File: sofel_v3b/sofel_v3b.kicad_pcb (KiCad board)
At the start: 2 copper layers, 145.4 x 116.3 mm, 107 parts, among them J1 Pimaroni Trackball, J2 4PIN, J3 OLED, SW1 SW_PUSH_LED, SW10 SW_PUSH_LED, SW11 SW_PUSH_LED, SW12 SW_PUSH_LED, SW13 SW_PUSH_LED, SW14 SW_PUSH_LED, SW15 SW_PUSH_LED, SW16 SW_PUSH_LED, SW17 SW_PUSH_LED, SW18 SW_PUSH_LED, SW19 SW_PUSH_LED, SW2 SW_PUSH_LED, SW20 SW_PUSH_LED, SW21 SW_PUSH_LED, SW22 SW_PUSH_LED, SW23 SW_PUSH_LED, SW24 SW_PUSH_LED, SW25 Rotary_Encoder_Switch, SW26 SW_PUSH_LED, SW27 SW_PUSH_LED, SW28 SW_PUSH_LED, SW29 SW_PUSH_LED, SW3 SW_PUSH_LED, SW30 SW_PUSH_LED, SW4 SW_PUSH_LED, SW5 SW_PUSH_LED, SW6 SW_PUSH_LED, SW7 SW_PUSH_LED, SW8 SW_PUSH_LED, SW9 SW_PUSH_LED, U2 SN74AHCT1G125, U3 Pico

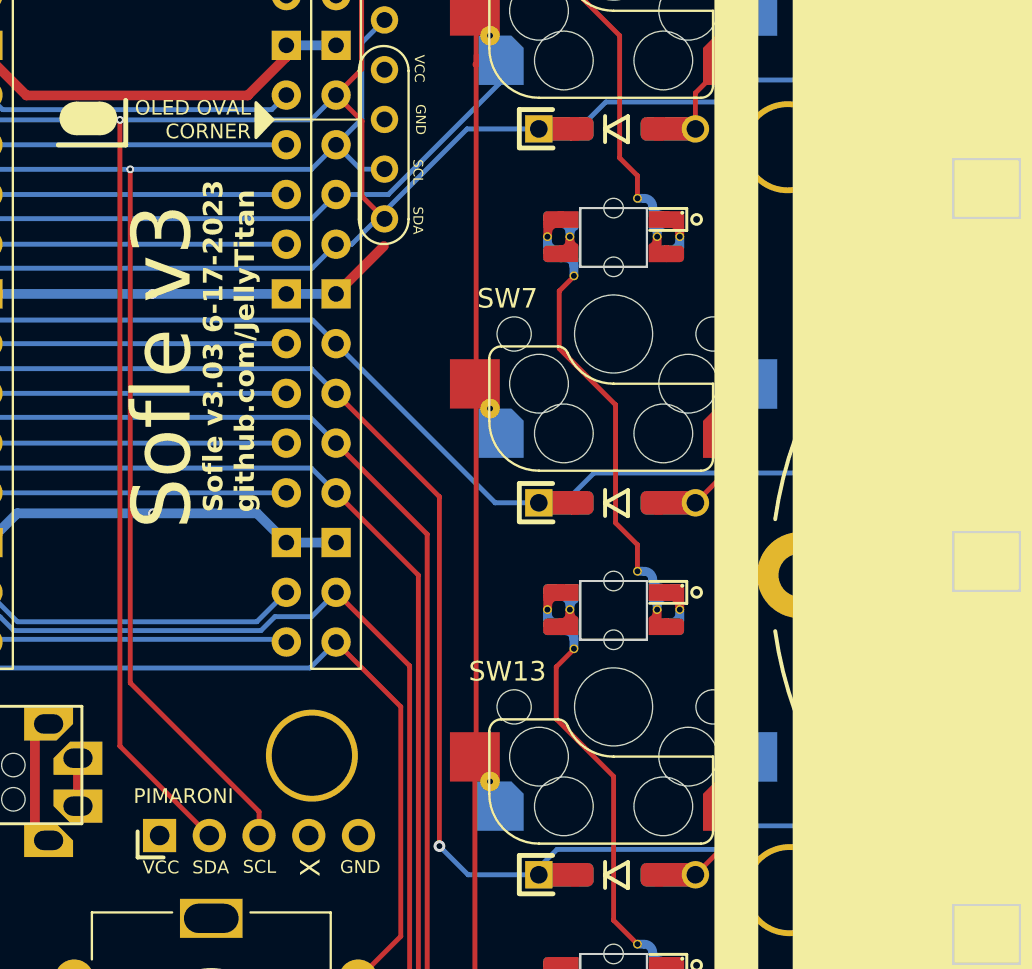
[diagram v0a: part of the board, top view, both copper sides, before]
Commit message: updated keyplate for alternate OLEDs
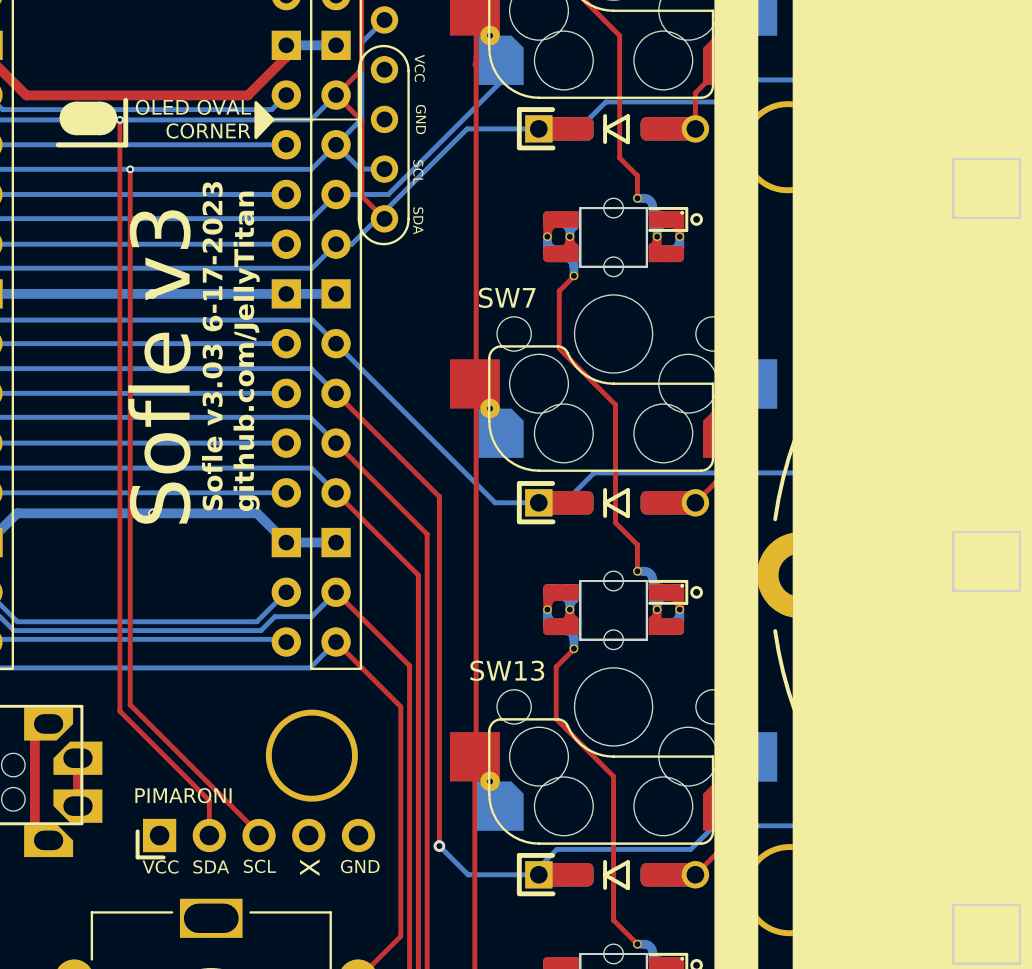
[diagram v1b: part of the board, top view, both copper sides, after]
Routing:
- net GND: track 94.8 -> 91.4 mm

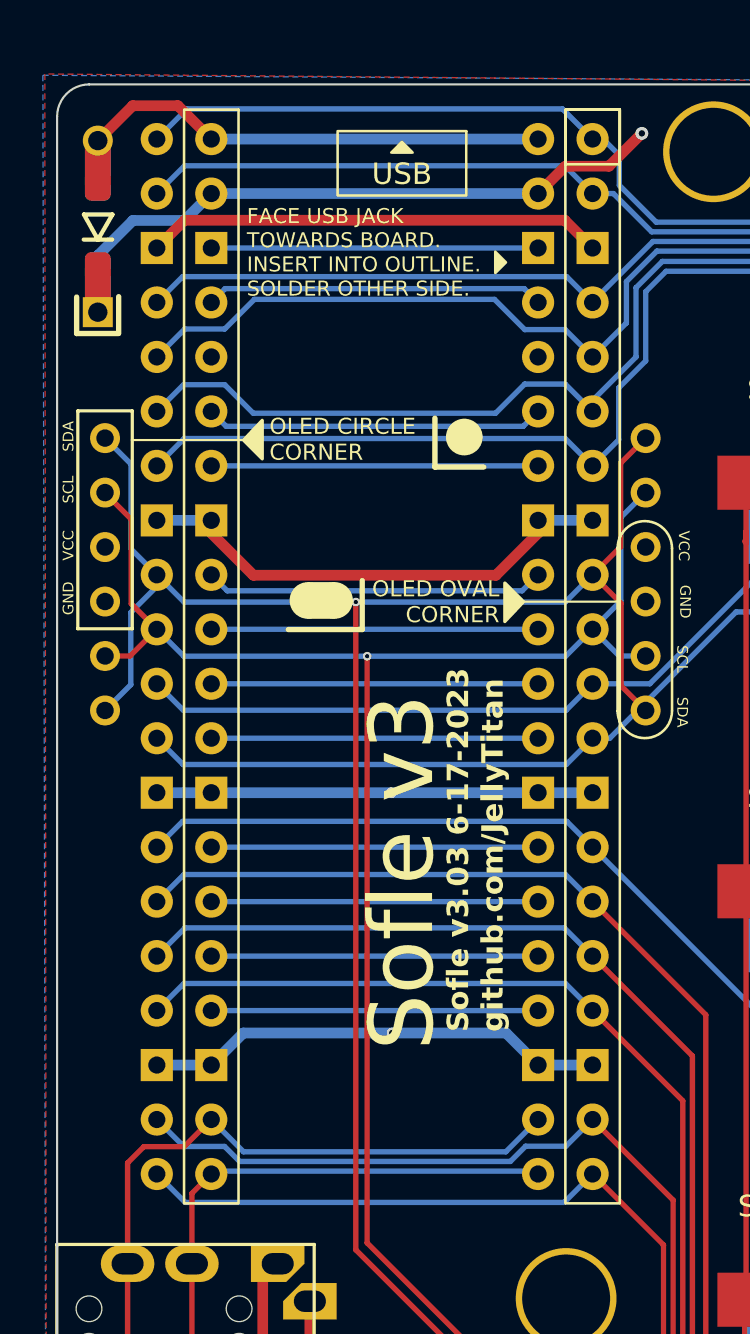
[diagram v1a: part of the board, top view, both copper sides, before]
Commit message: Flipped pico footrpint so buttons face up Removed pcb holes for pico buttons
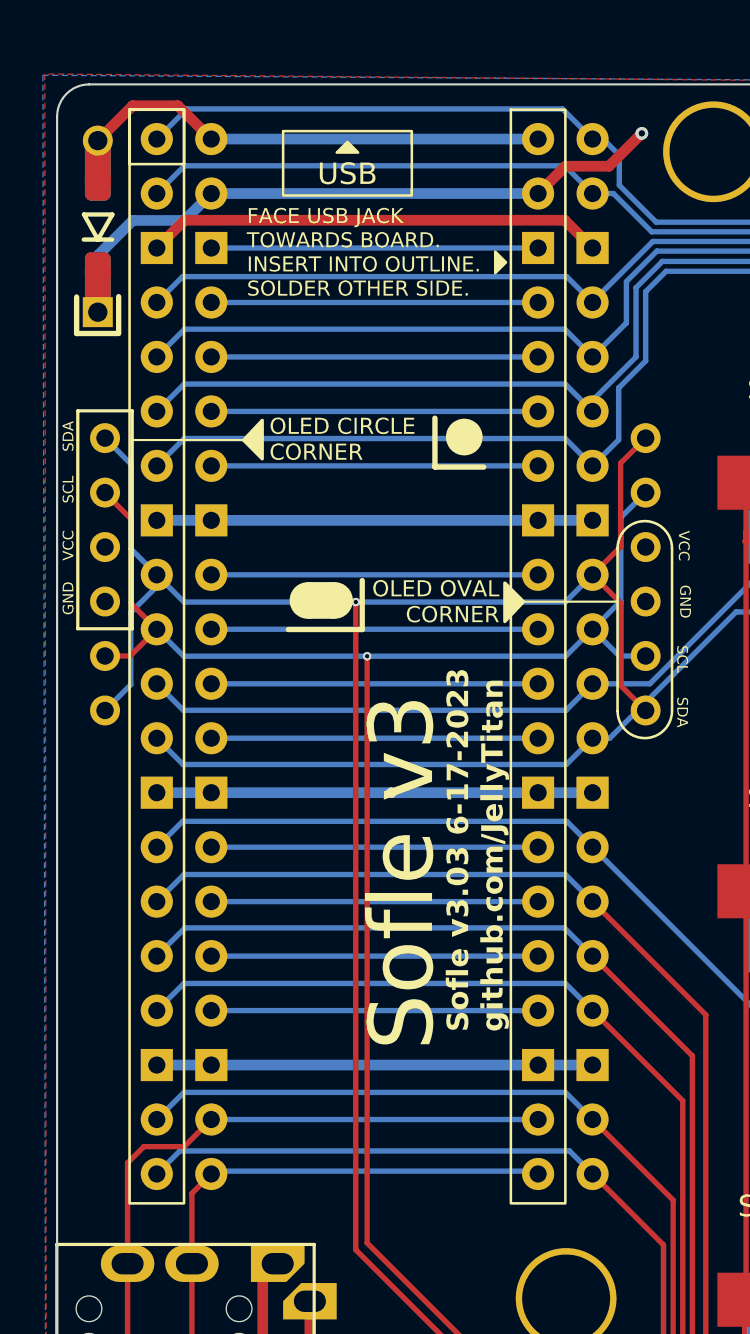
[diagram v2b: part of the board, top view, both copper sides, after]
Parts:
- U3: footprint sofle_v3b:RPi_Pico_SMD_TH - Junco -DS Sofle v3b v4 -> sofle_v3b:RPi_Pico_SMD_TH - Junco -DS Sofle v3b v3 nohole
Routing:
- net unconnected-(U3-3V3-Pad36): track 0.00 -> 15.2 mm
- net GND: track 91.4 -> 87.3 mm, vias 4 -> 3
- net RX: track 31.9 -> 30.6 mm
- net col2: track 215.2 -> 214.0 mm
- net col3: track 201.1 -> 200.0 mm
- net unconnected-(U3-GPIO27_ADC1-Pad32): track 15.9 -> 15.2 mm
- net unconnected-(U3-ADC_VREF-Pad35): track 15.8 -> 15.2 mm
- net ENCA: track 49.3 -> 48.8 mm
- net unconnected-(U3-3V3_EN-Pad37): track 15.8 -> 15.2 mm

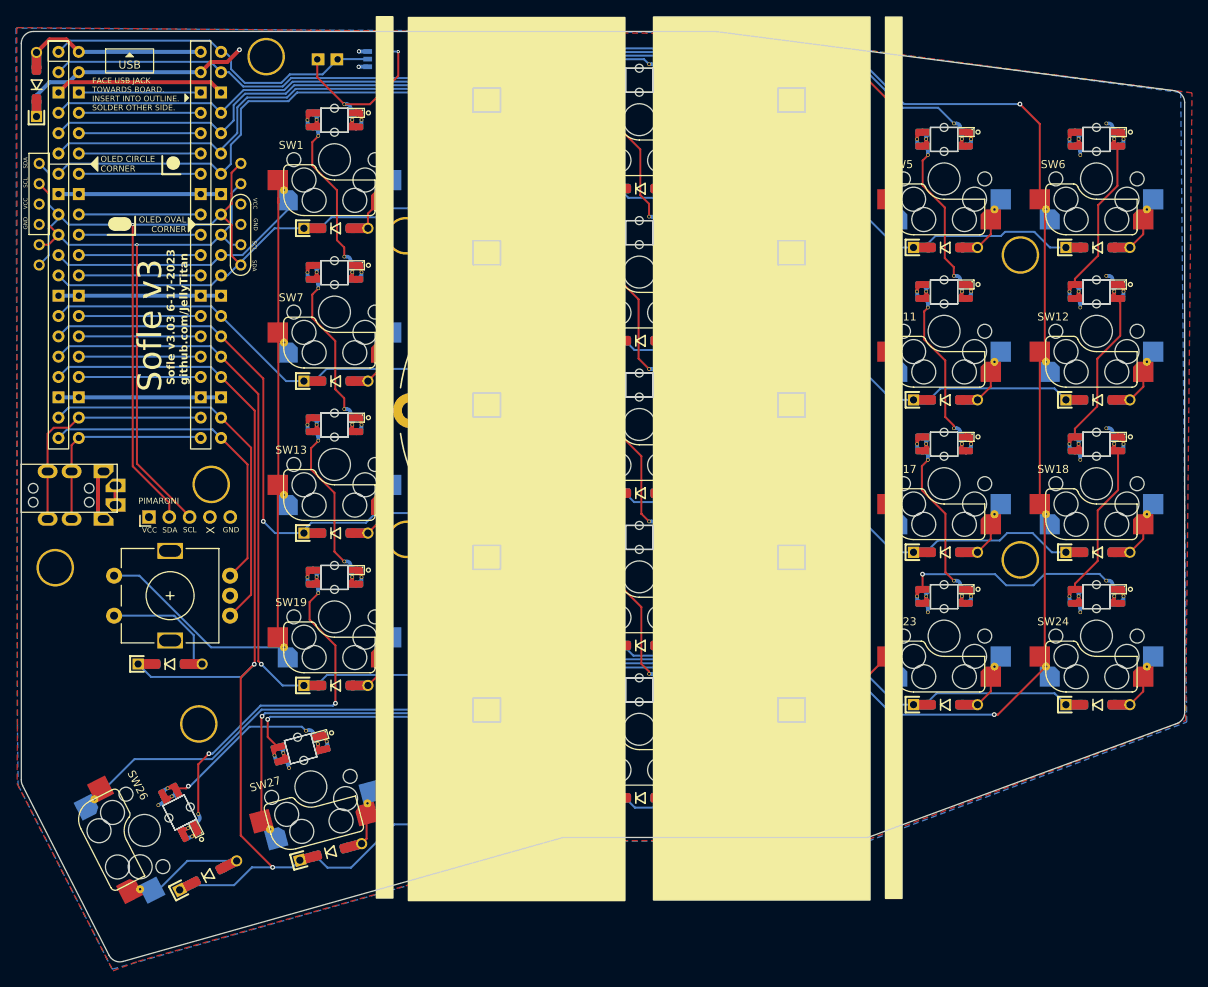
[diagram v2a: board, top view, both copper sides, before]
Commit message: Added solenoid and plates
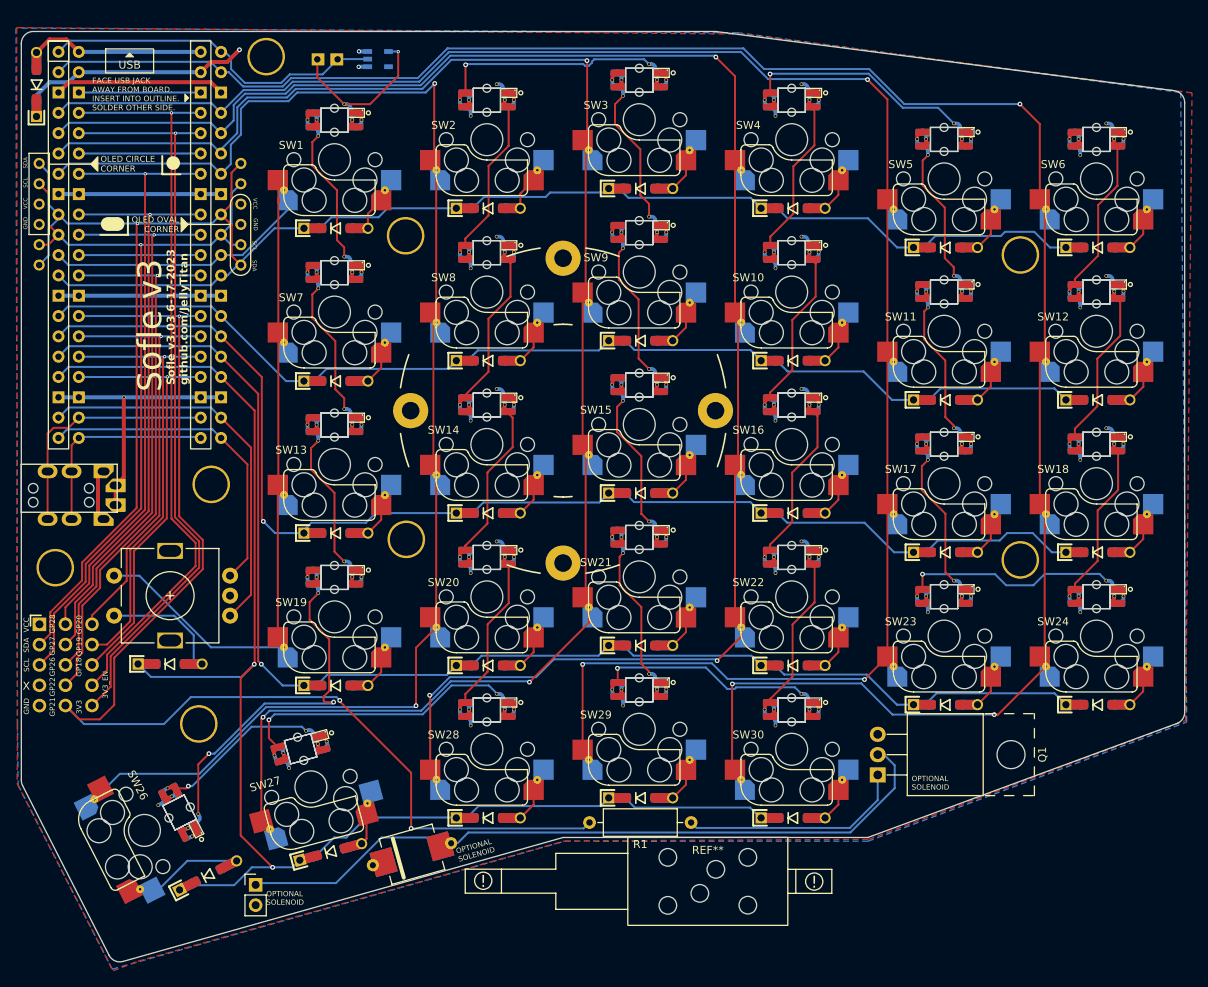
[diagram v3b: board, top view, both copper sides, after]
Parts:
- added D_SOL_1: MUR340S, sofle_v3b:MUR340S_IN4001_TH_HYBRID, F.Cu at (130.2, 136.8)
- added J5: Conn_01x05_Socket, Connector_PinHeader_2.54mm:PinHeader_1x05_P2.54mm_Vertical, F.Cu at (86.9, 108.1)
- added J6: Conn_01x05_Socket, Connector_PinHeader_2.54mm:PinHeader_1x05_P2.54mm_Vertical, F.Cu at (90.2, 108.1)
- added J_SOL_1: Conn_01x02_Female, sofle_v3b:PinHeader_1x02_P2.54mm_Vertical, F.Cu at (110.7, 140.6)
- added Q1: TIP120, sofle_v3b:TO-220-3_Horizontal_TabUp, F.Cu at (188.5, 126.9)
- added R1: 1k, Resistor_THT:R_Axial_DIN0309_L9.0mm_D3.2mm_P12.70mm_Horizontal, F.Cu at (165.1, 132.9)
- added REF**: uxcell a14092600ux0438 solenoid, sofle_v3b:uxcell a14092600ux0438 solenoid, F.Cu at (167.2, 140.2)
- moved J1 19.2 mm to (83.7, 108.1), turned to 0 degrees
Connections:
- U3 pad 24: unconnected-(U3-GPIO18-Pad24) -> GP18
- U3 pad 25: SOLENOID_CONTROL -> GP19
- U3 pad 26: unconnected-(U3-GPIO20-Pad26) -> GP20
- U3 pad 27: unconnected-(U3-GPIO21-Pad27) -> GP21
- U3 pad 29: unconnected-(U3-GPIO22-Pad29) -> GP22
- U3 pad 31: unconnected-(U3-GPIO26_ADC0-Pad31) -> GP26
- U3 pad 32: unconnected-(U3-GPIO27_ADC1-Pad32) -> GP27
- U3 pad 34: unconnected-(U3-GPIO28_ADC2-Pad34) -> GP28
- U3 pad 36: unconnected-(U3-3V3-Pad36) -> 3V3
- U3 pad 37: unconnected-(U3-3V3_EN-Pad37) -> 3V3_EN
- U3 pad 38: unconnected-(U3-GND-Pad38) -> GND
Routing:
- net GP21: track 0.00 -> 156.3 mm, vias 0 -> 3
- net 3V3: track 0.00 -> 93.6 mm, vias 0 -> 1
- net 3V3_EN: track 0.00 -> 93.4 mm, vias 0 -> 1
- net Net-(J_SOL_1-Pin_1): track 0.00 -> 89.2 mm
- net GP28: track 0.00 -> 75.7 mm, vias 0 -> 1
- net GP26: track 0.00 -> 73.6 mm, vias 0 -> 1
- net GP27: track 0.00 -> 73.4 mm, vias 0 -> 1
- net GP22: track 0.00 -> 71.2 mm, vias 0 -> 1
- net GP19: track 0.00 -> 56.1 mm, vias 0 -> 1
- net GP18: track 0.00 -> 55.2 mm, vias 0 -> 1
- net GP20: track 0.00 -> 54.8 mm, vias 0 -> 1
- net Net-(Q1-B): track 0.00 -> 28.2 mm
- net GND: track 87.3 -> 114.0 mm
- net SCL: track 78.8 -> 99.9 mm
- net SDA: track 89.3 -> 108.4 mm
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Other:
- board text added: "3V3"
- board text added: "3V3_EN"
- board text added: "FACE USB JACK AWAY FROM BOARD. INSERT INTO OUTLINE. SOLDER OTHER SIDE."
- board text added: "GP18"
- board text added: "GP19"
- board text added: "GP20"
- board text added: "GP21"
- board text added: "GP22"
- board text added: "GP26"
- board text added: "GP27"
- board text added: "GP28"
- board text added: "OPTIONAL SOLENOID"
- board text removed: "FACE USB JACK TOWARDS BOARD. INSERT INTO OUTLINE. SOLDER OTHER SIDE."
